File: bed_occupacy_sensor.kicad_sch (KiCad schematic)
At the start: 5 parts, among them J1 bedside_wife, J2 bedside_husband, U1 mini_esp32

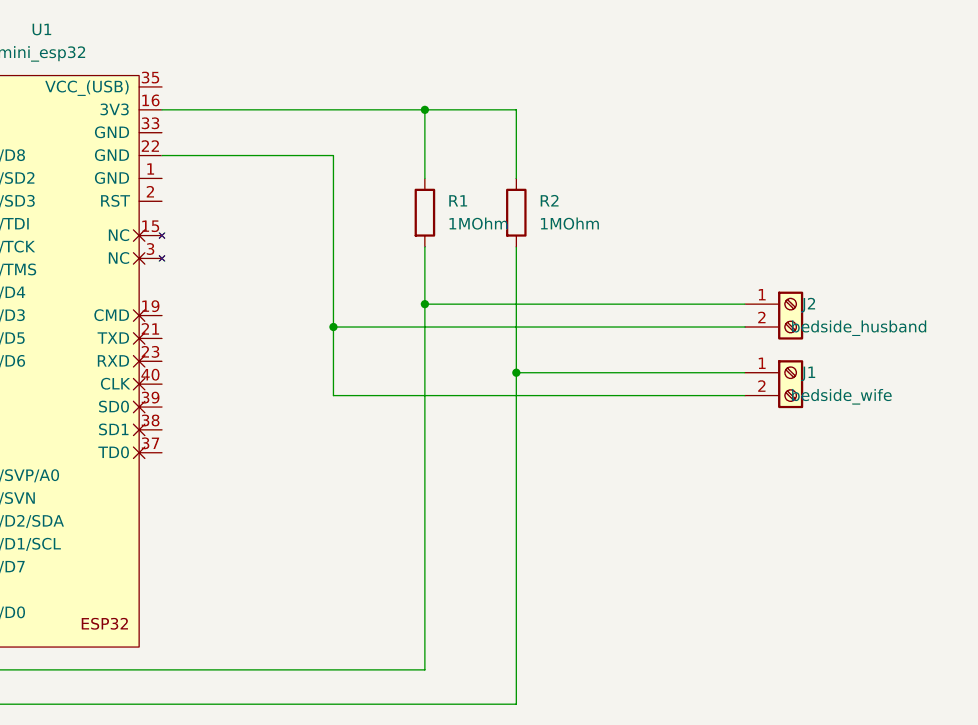
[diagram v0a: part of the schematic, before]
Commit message: new pcb design all GND connected to ground plane
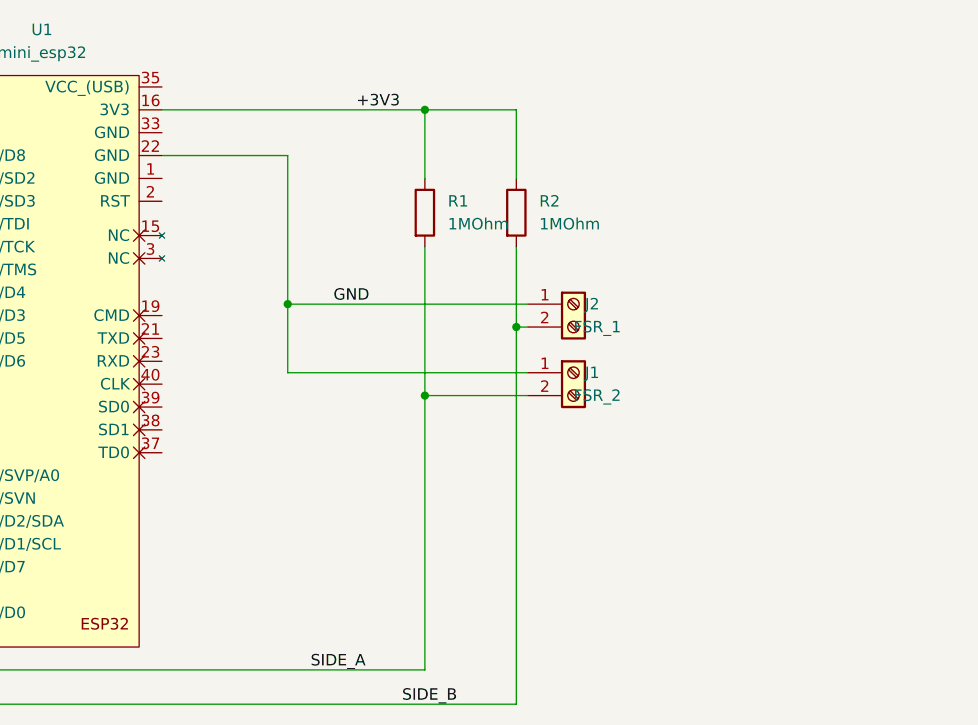
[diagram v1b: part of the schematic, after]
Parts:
- J1: value bedside_wife -> FSR_2
- J2: value bedside_husband -> FSR_1
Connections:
- net SIDE_B: now reaches R2.2, U1.11 (IO_34)
- net SIDE_B: now also J2.2 (Pin_2); no longer J1.1 (Pin_1)
- net +3V3: now reaches R1.1, R2.1, U1.16 (3V3)
- net SIDE_A: now reaches R1.2, U1.7 (IO_35)
- net SIDE_A: now also J1.2 (Pin_2); no longer J2.1 (Pin_1)
- new net GND: J1.1 (Pin_1), J2.1 (Pin_1), U1.22 (GND)
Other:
- moved on the sheet: J1, J2
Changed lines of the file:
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@@
   (junction (at 113.03 26.67) (diameter 0) (color 0 0 0 0)
   )
-  (junction (at 102.87 50.8) (diameter 0) (color 0 0 0 0)
-  )
-  (junction (at 113.03 48.26) (diameter 0) (color 0 0 0 0)
-  )
-  (junction (at 123.19 55.88) (diameter 0) (color 0 0 0 0)
-  )
-  (wire (pts (xy 148.59 58.42) (xy 102.87 58.42))
-    (stroke (width 0) (type default) (color 0 0 0 0))
+  (junction (at 97.79 48.26) (diameter 0) (color 0 0 0 0)
+  )
+  (junction (at 123.19 50.8) (diameter 0) (color 0 0 0 0)
+  )
+  (junction (at 113.03 58.42) (diameter 0) (color 0 0 0 0)
   )
   (wire (pts (xy 123.19 92.71) (xy 48.26 92.71))
     (stroke (width 0) (type default) (color 0 0 0 0))
   )
-  (wire (pts (xy 148.59 48.26) (xy 113.03 48.26))
-    (stroke (width 0) (type default) (color 0 0 0 0))
-  )
-  (wire (pts (xy 83.82 31.75) (xy 102.87 31.75))
-    (stroke (width 0) (type default) (color 0 0 0 0))
-  )
-  (wire (pts (xy 113.03 41.91) (xy 113.03 48.26))
+  (wire (pts (xy 124.46 55.88) (xy 97.79 55.88))
+    (stroke (width 0) (type default) (color 0 0 0 0))
+  )
+  (wire (pts (xy 113.03 41.91) (xy 113.03 58.42))
     (stroke (width 0) (type default) (color 0 0 0 0))
   )
@@
     (stroke (width 0) (type default) (color 0 0 0 0))
   )
+  (wire (pts (xy 123.19 50.8) (xy 124.46 50.8))
+    (stroke (width 0) (type default) (color 0 0 0 0))
+  )
   (wire (pts (xy 52.07 88.9) (xy 52.07 64.77))
     (stroke (width 0) (type default) (color 0 0 0 0))
   )
-  (wire (pts (xy 123.19 55.88) (xy 148.59 55.88))
-    (stroke (width 0) (type default) (color 0 0 0 0))
-  )
   (wire (pts (xy 113.03 26.67) (xy 113.03 34.29))
     (stroke (width 0) (type default) (color 0 0 0 0))
@@
     (stroke (width 0) (type default) (color 0 0 0 0))
   )
-  (wire (pts (xy 113.03 48.26) (xy 113.03 88.9))
+  (wire (pts (xy 113.03 58.42) (xy 113.03 88.9))
     (stroke (width 0) (type default) (color 0 0 0 0))
   )
@@
     (stroke (width 0) (type default) (color 0 0 0 0))
   )
-  (wire (pts (xy 123.19 41.91) (xy 123.19 55.88))
+  (wire (pts (xy 123.19 41.91) (xy 123.19 50.8))
+    (stroke (width 0) (type default) (color 0 0 0 0))
+  )
+  (wire (pts (xy 97.79 31.75) (xy 83.82 31.75))
+    (stroke (width 0) (type default) (color 0 0 0 0))
+  )
+  (wire (pts (xy 113.03 58.42) (xy 124.46 58.42))
+    (stroke (width 0) (type default) (color 0 0 0 0))
+  )
+  (wire (pts (xy 123.19 50.8) (xy 123.19 92.71))
     (stroke (width 0) (type default) (color 0 0 0 0))
   )
@@
     (stroke (width 0) (type default) (color 0 0 0 0))
   )
-  (wire (pts (xy 102.87 50.8) (xy 102.87 58.42))
-    (stroke (width 0) (type default) (color 0 0 0 0))
-  )
-  (wire (pts (xy 102.87 50.8) (xy 148.59 50.8))
-    (stroke (width 0) (type default) (color 0 0 0 0))
-  )
-  (wire (pts (xy 123.19 55.88) (xy 123.19 92.71))
-    (stroke (width 0) (type default) (color 0 0 0 0))
-  )
-  (wire (pts (xy 102.87 31.75) (xy 102.87 50.8))
-    (stroke (width 0) (type default) (color 0 0 0 0))
+  (wire (pts (xy 124.46 48.26) (xy 97.79 48.26))
+    (stroke (width 0) (type default) (color 0 0 0 0))
+  )
+  (wire (pts (xy 97.79 48.26) (xy 97.79 31.75))
+    (stroke (width 0) (type default) (color 0 0 0 0))
+  )
+  (wire (pts (xy 97.79 55.88) (xy 97.79 48.26))
+    (stroke (width 0) (type default) (color 0 0 0 0))
+  )
+  (label "SIDE_A" (at 100.33 88.9 0)
+    (effects (font (size 1.27 1.27)) (justify left bottom))
+  )
+  (label "GND" (at 102.87 48.26 0)
+    (effects (font (size 1.27 1.27)) (justify left bottom))
+  )
+  (label "SIDE_B" (at 110.49 92.71 0)
+    (effects (font (size 1.27 1.27)) (justify left bottom))
+  )
+  (label "+3V3" (at 105.41 26.67 0)
+    (effects (font (size 1.27 1.27)) (justify left bottom))
   )
   (symbol (lib_id "ESP32_Mini:mini_esp32") (at 69.85 21.59 0) (unit 1)
@@
     (pin "2")
   )
-  (symbol (lib_id "Connector:Screw_Terminal_01x02") (at 153.67 48.26 0) (unit 1)
+  (symbol (lib_id "Connector:Screw_Terminal_01x02") (at 129.54 48.26 0) (unit 1)
     (in_bom yes) (on_board yes)
-    (property "Reference" "J2" (id 0) (at 154.94 48.2599 0)
-      (effects (font (size 1.27 1.27)) (justify left))
-    )
-    (property "Value" "bedside_husband" (id 1) (at 153.67 50.8 0)
-      (effects (font (size 1.27 1.27)) (justify left))
-    )
-    (property "Footprint" "TerminalBlock:TerminalBlock_Altech_AK300-2_P5.00mm" (id 2) (at 153.67 48.26 0)
-      (effects (font (size 1.27 1.27)) hide)
-    )
-    (property "Datasheet" "~" (id 3) (at 153.67 48.26 0)
+    (property "Reference" "J2" (id 0) (at 130.81 48.2599 0)
+      (effects (font (size 1.27 1.27)) (justify left))
+    )
+    (property "Value" "FSR_1" (id 1) (at 129.54 50.8 0)
+      (effects (font (size 1.27 1.27)) (justify left))
+    )
+    (property "Footprint" "TerminalBlock:TerminalBlock_Altech_AK300-2_P5.00mm" (id 2) (at 129.54 48.26 0)
+      (effects (font (size 1.27 1.27)) hide)
+    )
+    (property "Datasheet" "~" (id 3) (at 129.54 48.26 0)
       (effects (font (size 1.27 1.27)) hide)
     )
@@
     (pin "2")
   )
-  (symbol (lib_id "Connector:Screw_Terminal_01x02") (at 153.67 55.88 0) (unit 1)
+  (symbol (lib_id "Connector:Screw_Terminal_01x02") (at 129.54 55.88 0) (unit 1)
     (in_bom yes) (on_board yes)
-    (property "Reference" "J1" (id 0) (at 154.94 55.8799 0)
-      (effects (font (size 1.27 1.27)) (justify left))
-    )
-    (property "Value" "bedside_wife" (id 1) (at 153.67 58.42 0)
-      (effects (font (size 1.27 1.27)) (justify left))
-    )
-    (property "Footprint" "TerminalBlock:TerminalBlock_Altech_AK300-2_P5.00mm" (id 2) (at 153.67 55.88 0)
-      (effects (font (size 1.27 1.27)) hide)
-    )
-    (property "Datasheet" "~" (id 3) (at 153.67 55.88 0)
+    (property "Reference" "J1" (id 0) (at 130.81 55.8799 0)
+      (effects (font (size 1.27 1.27)) (justify left))
+    )
+    (property "Value" "FSR_2" (id 1) (at 129.54 58.42 0)
+      (effects (font (size 1.27 1.27)) (justify left))
+    )
+    (property "Footprint" "TerminalBlock:TerminalBlock_Altech_AK300-2_P5.00mm" (id 2) (at 129.54 55.88 0)
+      (effects (font (size 1.27 1.27)) hide)
+    )
+    (property "Datasheet" "~" (id 3) (at 129.54 55.88 0)
       (effects (font (size 1.27 1.27)) hide)
     )
@@
   (symbol_instances
     (path "/cffda6a0-0f23-4acc-9bf9-5bf7a873e0dc"
-      (reference "J1") (unit 1) (value "bedside_wife") (footprint "TerminalBlock:TerminalBlock_Altech_AK300-2_P5.00mm")
+      (reference "J1") (unit 1) (value "FSR_2") (footprint "TerminalBlock:TerminalBlock_Altech_AK300-2_P5.00mm")
     )
     (path "/3bd0023a-f089-407e-a041-ef365f6d614d"
-      (reference "J2") (unit 1) (value "bedside_husband") (footprint "TerminalBlock:TerminalBlock_Altech_AK300-2_P5.00mm")
+      (reference "J2") (unit 1) (value "FSR_1") (footprint "TerminalBlock:TerminalBlock_Altech_AK300-2_P5.00mm")
     )
     (path "/34513afa-65fd-4100-9268-ca482871ddd0"

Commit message: Save-Changes again
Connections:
- net GND: now also U1.1 (GND), U1.33 (GND)
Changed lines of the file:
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@@
   (junction (at 123.19 50.8) (diameter 0) (color 0 0 0 0)
+  )
+  (junction (at 86.36 31.75) (diameter 0) (color 0 0 0 0)
   )
   (junction (at 113.03 58.42) (diameter 0) (color 0 0 0 0)
@@
     (stroke (width 0) (type default) (color 0 0 0 0))
   )
+  (wire (pts (xy 83.82 34.29) (xy 86.36 34.29))
+    (stroke (width 0) (type default) (color 0 0 0 0))
+  )
   (wire (pts (xy 124.46 55.88) (xy 97.79 55.88))
+    (stroke (width 0) (type default) (color 0 0 0 0))
+  )
+  (wire (pts (xy 86.36 31.75) (xy 83.82 31.75))
     (stroke (width 0) (type default) (color 0 0 0 0))
   )
@@
     (stroke (width 0) (type default) (color 0 0 0 0))
   )
+  (wire (pts (xy 83.82 29.21) (xy 86.36 29.21))
+    (stroke (width 0) (type default) (color 0 0 0 0))
+  )
   (wire (pts (xy 123.19 26.67) (xy 123.19 34.29))
+    (stroke (width 0) (type default) (color 0 0 0 0))
+  )
+  (wire (pts (xy 86.36 29.21) (xy 86.36 31.75))
     (stroke (width 0) (type default) (color 0 0 0 0))
   )
@@
     (stroke (width 0) (type default) (color 0 0 0 0))
   )
-  (wire (pts (xy 97.79 31.75) (xy 83.82 31.75))
+  (wire (pts (xy 97.79 31.75) (xy 86.36 31.75))
     (stroke (width 0) (type default) (color 0 0 0 0))
   )
@@
     (stroke (width 0) (type default) (color 0 0 0 0))
   )
+  (wire (pts (xy 86.36 34.29) (xy 86.36 31.75))
+    (stroke (width 0) (type default) (color 0 0 0 0))
+  )

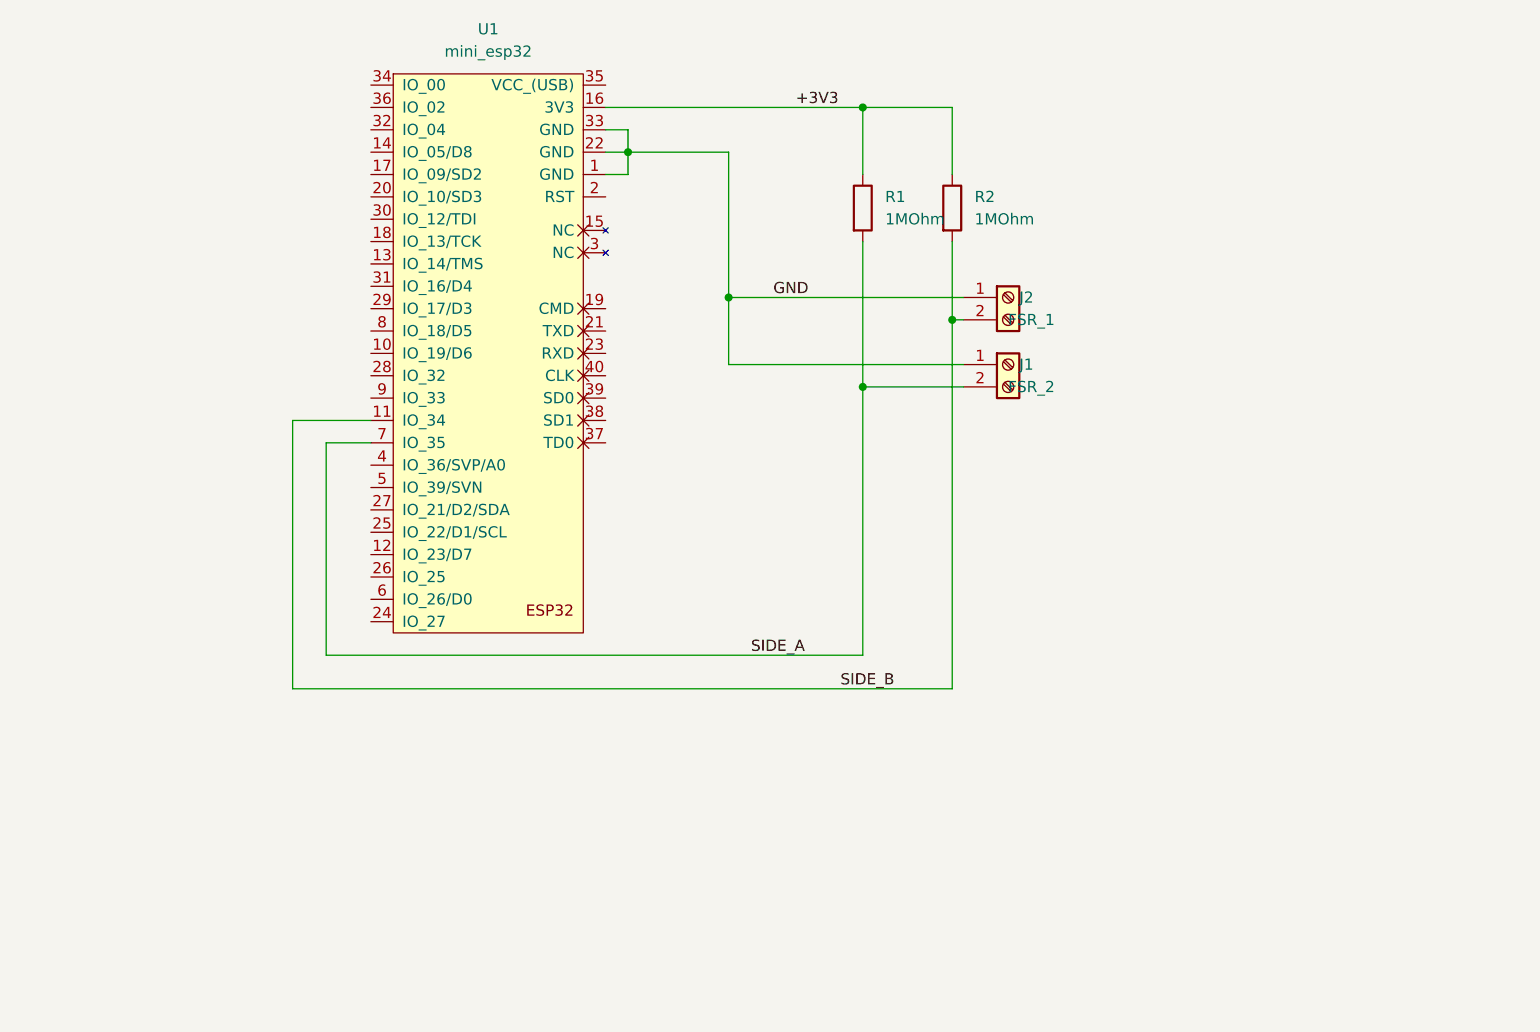
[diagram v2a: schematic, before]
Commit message: Updated to design ESP32 flipped to get smaller PCB added QR-Code for Project-Link
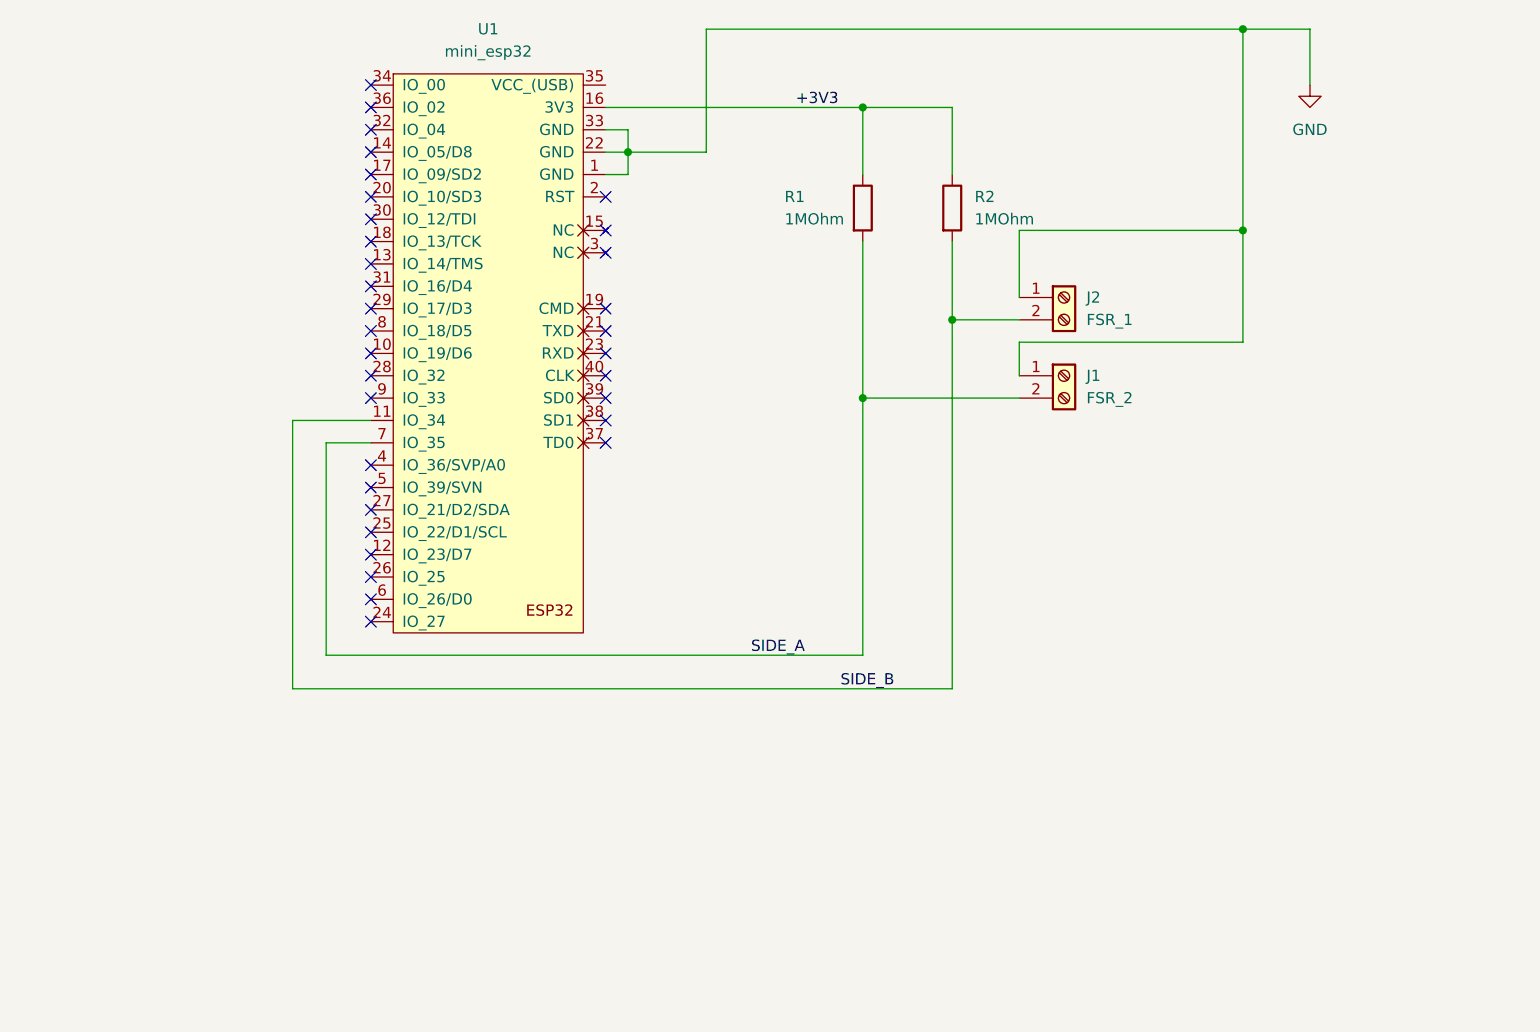
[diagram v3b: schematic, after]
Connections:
- no-connect marks 0 -> 33
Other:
- moved on the sheet: J1, J2

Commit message: complete redesign added terminal-block for getting power from external powersupply flipped esp header for getting smaller kicad_pcb added descriptions for pins and QR code
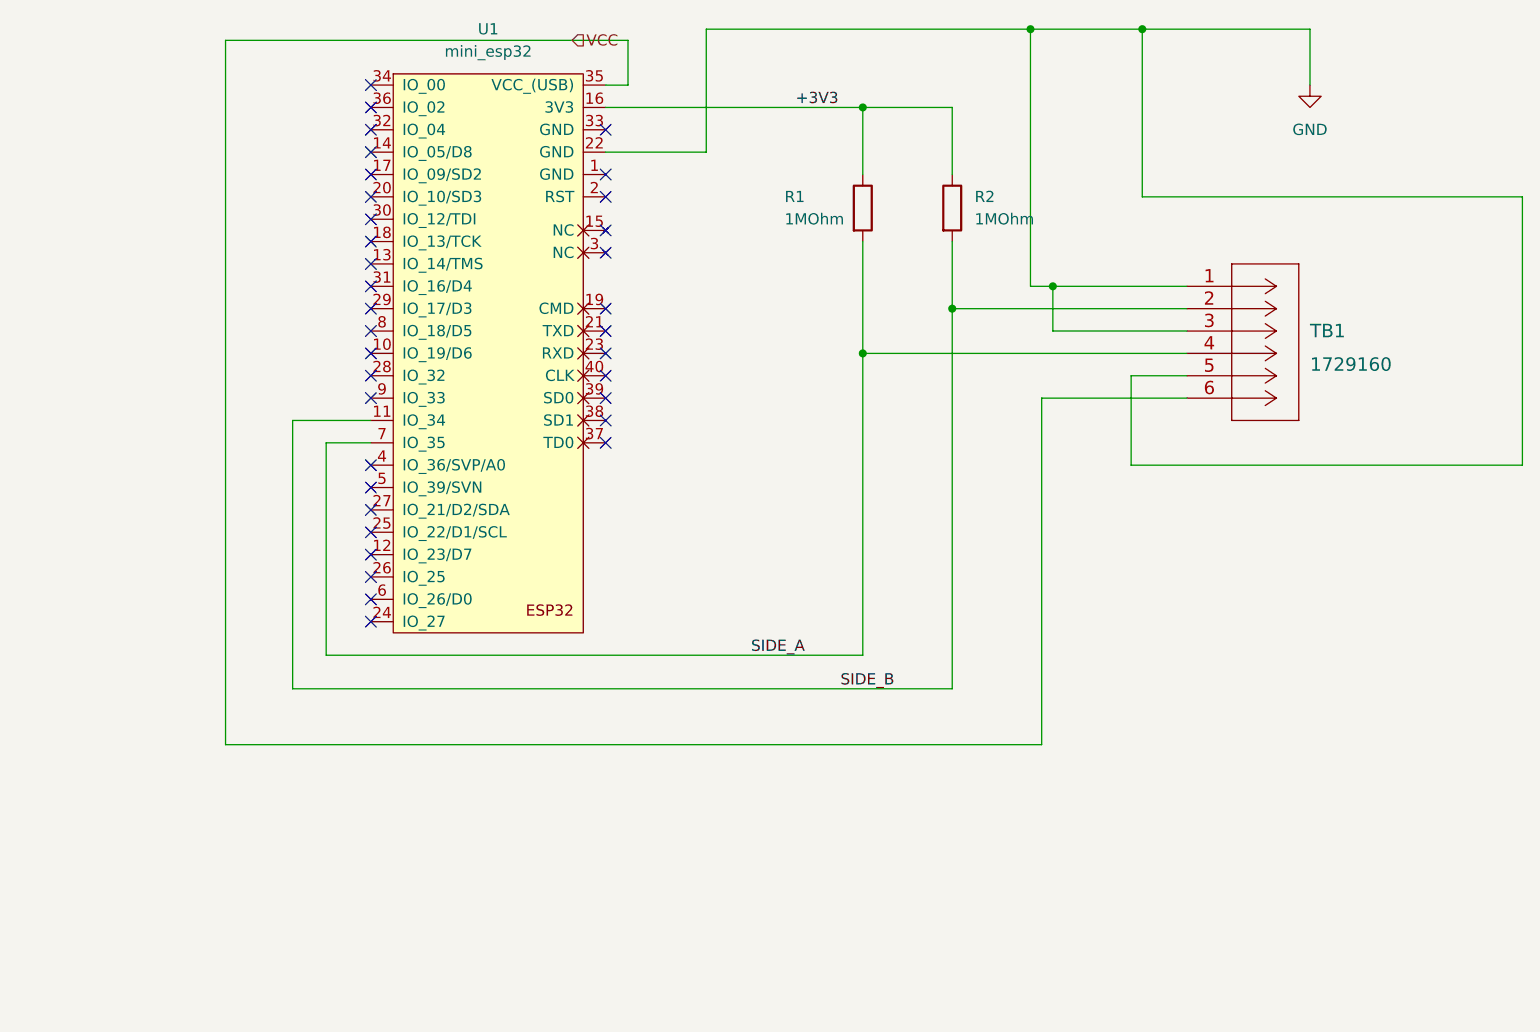
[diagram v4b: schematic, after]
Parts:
- removed J1: FSR_2, TerminalBlock:TerminalBlock_Altech_AK300-2_P5.00mm, symbol Connector:Screw_Terminal_01x02
- removed J2: FSR_1, TerminalBlock:TerminalBlock_Altech_AK300-2_P5.00mm, symbol Connector:Screw_Terminal_01x02
- added TB1: 1729160, TerminalBlock_Phoenix:TerminalBlock_Phoenix_MKDS-1,5-6-5.08_1x06_P5.08mm_Horizontal, symbol phoenixcontact_1729160:1729160
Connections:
- net GND: now also TB1.1, TB1.3, TB1.5; no longer U1.1 (GND), U1.33 (GND)
- net SIDE_A: now also TB1.4
- net SIDE_B: now also TB1.2
- net VCC: now reaches U1.35 (VCC_(USB))
- net VCC: now also TB1.6
- no-connect marks 33 -> 35
